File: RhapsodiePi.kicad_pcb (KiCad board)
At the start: 2 copper layers, 85.2 x 56.1 mm, 209 parts, among them J1 Micro_SD_Card_Det, J2 Conn_02x05_Odd_Even, J3 USB_A_Stacked, J4 USB_A_Stacked, J6 RJ45_HR913550A, J7 AudioJack4, U1 MT3420C-mt3420c, U11 LM4871, U13 TPS65185RGZR, U2 MT3420C-mt3420c, U3 MT3420C-mt3420c, U4 X1000, U5 AP6212, U6 FE2.1, U7 RTL8201F, U8 M25PX32-VMW, U9 TFP410PAP, X1 SG-3030CM, Y1 12MHz, Y2 24MHz, Y3 32.768kHz

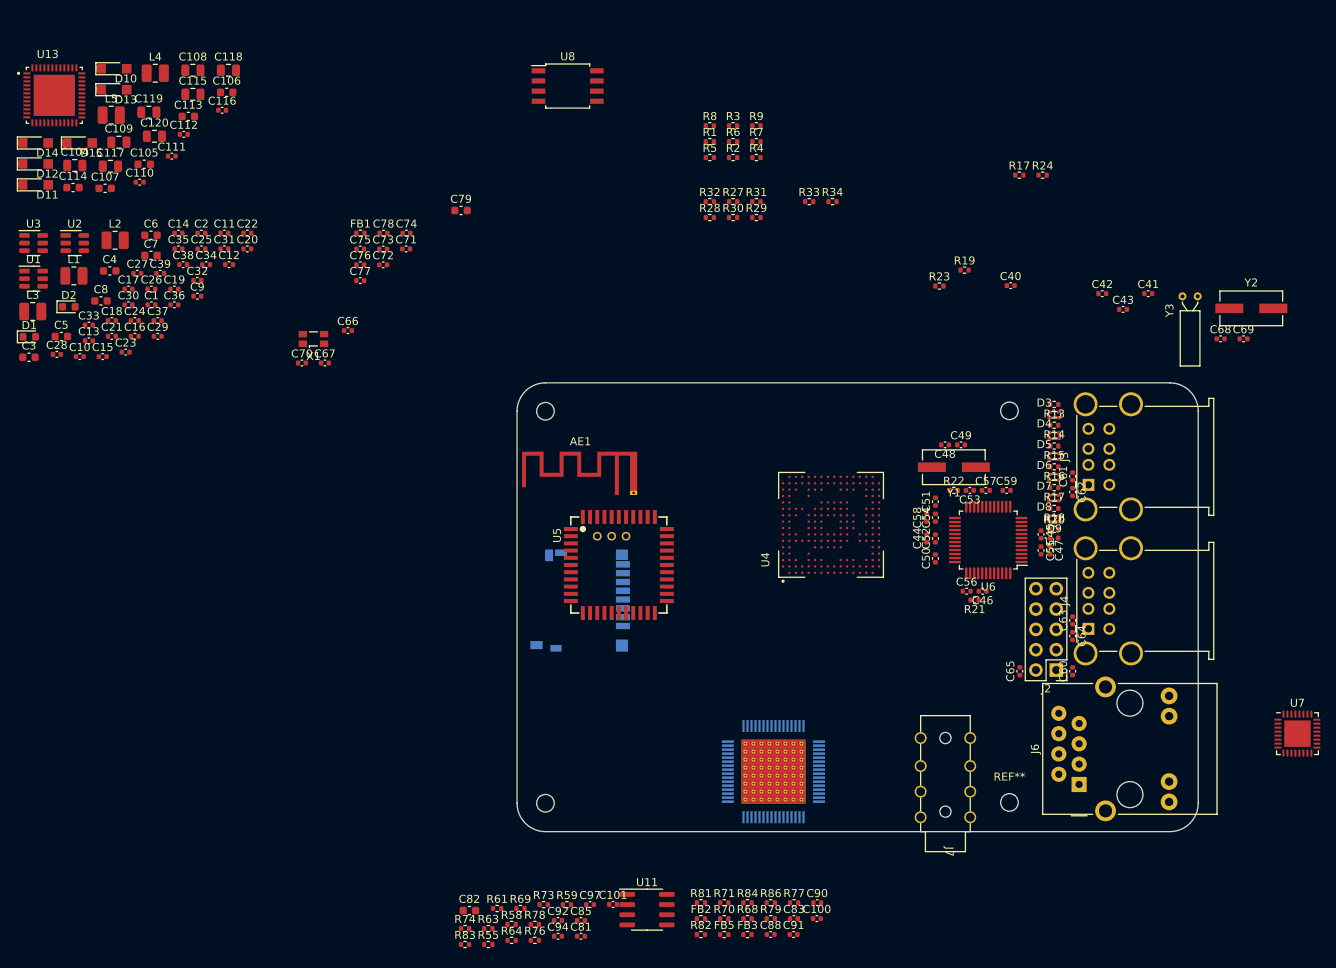
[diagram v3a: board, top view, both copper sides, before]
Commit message: Display Update
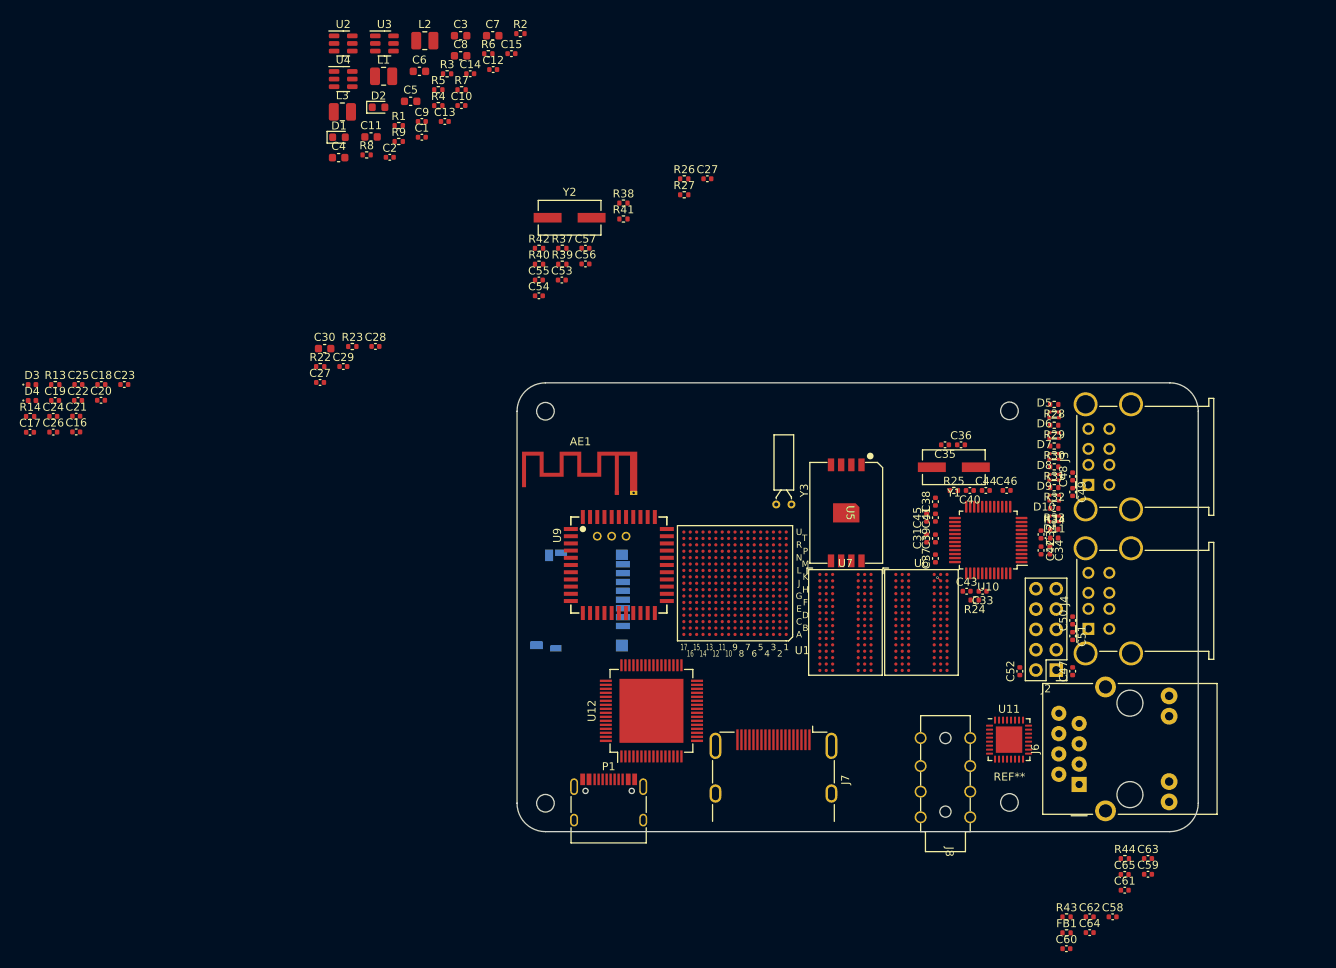
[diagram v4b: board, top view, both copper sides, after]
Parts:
- removed C100, C101, C73, C74, C85: 1µ, Capacitor_SMD:C_0402_1005Metric
- removed C104, C108, C109, C115, C117, C118, C119, C120: 4µ7, Capacitor_SMD:C_0805_2012Metric
- removed C105, C106, C107, C113, C114, C79, C82: 22µ, Capacitor_SMD:C_0603_1608Metric
- removed C110, C116, C71, C72, C75, C76, C77, C78, C81: 100n, Capacitor_SMD:C_0402_1005Metric
- removed C111, C112: 10n, Capacitor_SMD:C_0402_1005Metric
- removed the C27 at (36.8, 50.7)
- removed the C31 at (47.7, 47.6)
- removed the C32 at (44.3, 51.5)
- removed the C33 at (30.8, 57.1)
- removed the C34 at (45.4, 49.6)
- removed the C35 at (42.0, 47.6)
- removed the C36 at (41.5, 54.6)
- removed the C37 at (39.4, 56.6)
- removed the C38 at (42.6, 49.6)
- removed the C39 at (39.7, 50.7)
- removed the C40 at (146.0, 52.2)
- removed the C41 at (163.2, 53.2)
- removed the C42 at (157.5, 53.2)
- removed the C43 at (160.1, 55.2)
- removed C66, C67, C68, C69, C70: C, Capacitor_SMD:C_0402_1005Metric
- removed C83, C94, C97: 1n, Capacitor_SMD:C_0402_1005Metric
- removed C88, C90, C91, C92: 220p, Capacitor_SMD:C_0402_1005Metric
- removed the D10 at (33.9, 25.1)
- removed the D11 at (24.1, 39.6)
- removed D12, D13, D14, D15: D_Schottky, TheBrutzlers_Lib:SOD-123FL
- removed FB2, FB3, FB5: FerriteBead, Resistor_SMD:R_0402_1005Metric
- removed L4: 2µ2, Inductor_SMD:L_1008_2520Metric
- removed L5: 4µ7, Inductor_SMD:L_1008_2520Metric
- removed R17: 1K, Resistor_SMD:R_0402_1005Metric
- removed R19: 43.2, Resistor_SMD:R_0402_1005Metric
- removed the R24 at (150.0, 38.4)
- removed the R28 at (108.4, 43.7)
- removed the R29 at (114.2, 43.7)
- removed the R30 at (111.3, 43.7)
- removed the R31 at (114.2, 41.7)
- removed the R32 at (108.4, 41.7)
- removed the R33 at (120.8, 41.7)
- removed the R34 at (123.7, 41.7)
- removed R55: 2K2, Resistor_SMD:R_0402_1005Metric
- removed R58, R59, R61, R63, R64, R68, R69, R70, R71: 2K7, Resistor_SMD:R_0402_1005Metric
- removed R73, R74, R76, R81, R82: 10K, Resistor_SMD:R_0402_1005Metric
- removed R77, R78, R79: 20K, Resistor_SMD:R_0402_1005Metric
- removed R83, R84, R86: 0R, Resistor_SMD:R_0402_1005Metric
- removed U13: TPS65185RGZR, TheBrutzlers_Lib:QFN50P700X700X100-49N
- removed U8: M25PX32-VMW, Package_SO:SOIC-8W_5.3x5.3mm_P1.27mm
- removed the U9 at (116.3, 113.0)
- removed X1: SG-3030CM, Oscillator:Oscillator_SMD_SeikoEpson_SG3030CM
- added C27: 1µ, Capacitor_SMD:C_0402_1005Metric, F.Cu at (59.7, 64.3)
- added C27: 1µ, Capacitor_SMD:C_0402_1005Metric, F.Cu at (108.1, 38.8)
- added C53: C, Capacitor_SMD:C_0402_1005Metric, F.Cu at (89.9, 51.5)
- added C54: C, Capacitor_SMD:C_0402_1005Metric, F.Cu at (87.0, 53.5)
- added C55: C, Capacitor_SMD:C_0402_1005Metric, F.Cu at (87.0, 51.5)
- added C56: C, Capacitor_SMD:C_0402_1005Metric, F.Cu at (92.8, 49.5)
- added C57: C, Capacitor_SMD:C_0402_1005Metric, F.Cu at (92.8, 47.5)
- added C58: 100n, Capacitor_SMD:C_0402_1005Metric, F.Cu at (158.8, 131.1)
- added C59: 100n, Capacitor_SMD:C_0402_1005Metric, F.Cu at (163.2, 125.8)
- added C60: 1µ, Capacitor_SMD:C_0402_1005Metric, F.Cu at (153.0, 135.1)
- added C61: 1µ, Capacitor_SMD:C_0402_1005Metric, F.Cu at (160.3, 127.8)
- added C62: 100n, Capacitor_SMD:C_0402_1005Metric, F.Cu at (155.9, 131.1)
- added C63: 100n, Capacitor_SMD:C_0402_1005Metric, F.Cu at (163.2, 123.8)
- added C64: 100n, Capacitor_SMD:C_0402_1005Metric, F.Cu at (155.9, 133.1)
- added C65: 100n, Capacitor_SMD:C_0402_1005Metric, F.Cu at (160.3, 125.8)
- added D3: LED, LED_SMD:LED_0402_1005Metric, F.Cu at (23.7, 64.6)
- added D4: LED, LED_SMD:LED_0402_1005Metric, F.Cu at (23.7, 66.6)
- added J7: HDMI_A, Connector_HDMI:HDMI_A_Molex_208658-1001_Horizontal, F.Cu at (116.3, 112.2)
- added P1: USB_C_Plug, Connector_USB:USB_C_Receptacle_HRO_TYPE-C-31-M-12, F.Cu at (95.8, 118.0)
- added R13: 1K, Resistor_SMD:R_0402_1005Metric, F.Cu at (26.6, 64.6)
- added R14: 1K, Resistor_SMD:R_0402_1005Metric, F.Cu at (23.4, 68.5)
- added R22: 0R, Resistor_SMD:R_0402_1005Metric, F.Cu at (59.7, 62.3)
- added R26: 2K7, Resistor_SMD:R_0402_1005Metric, F.Cu at (105.2, 38.9)
- added R37: 1K, Resistor_SMD:R_0402_1005Metric, F.Cu at (90.0, 47.5)
- added R38: 100K, Resistor_SMD:R_0402_1005Metric, F.Cu at (97.6, 41.9)
- added R39: 100K, Resistor_SMD:R_0402_1005Metric, F.Cu at (90.0, 49.5)
- added R40: 1K, Resistor_SMD:R_0402_1005Metric, F.Cu at (87.0, 49.5)
- added R41: 100K, Resistor_SMD:R_0402_1005Metric, F.Cu at (97.6, 43.9)
- added R42: 1K, Resistor_SMD:R_0402_1005Metric, F.Cu at (87.0, 47.5)
- added R43: 1K, Resistor_SMD:R_0402_1005Metric, F.Cu at (153.0, 131.1)
- added R44: 1K, Resistor_SMD:R_0402_1005Metric, F.Cu at (160.3, 123.8)
- added U12: TFP410PAP, Package_QFP:HTQFP-64-1EP_10x10mm_P0.5mm_EP8x8mm, F.Cu at (101.1, 105.3)
- added U5: MKDN0xxxCL, TheBrutzlers_Lib:LGA-16_NAND, F.Cu at (125.5, 80.6)
- added U6: MT41K256M16TW, Package_BGA:BGA-96_9.0x13.0mm_Layout2x3x16_P0.8mm, F.Cu at (134.8, 94.3)
- C11, C30: value 100n -> 22µ; footprint Capacitor_SMD:C_0402_1005Metric -> Capacitor_SMD:C_0603_1608Metric
- C16, C24, C25, C26, C28: value 100n -> 1µ
- R23: value 2K7 -> 0R
- R5: value 200K -> 133K
- U1: value MT3420C-mt3420c -> IMX6UL; footprint Package_TO_SOT_SMD:SOT-23-6 -> TheBrutzlers_Lib:IMX6UL_BGA289
- U11: value LM4871 -> RTL8201F; footprint Package_SO:SOIC-8_3.9x4.9mm_P1.27mm -> Package_DFN_QFN:QFN-32-1EP_5x5mm_P0.5mm_EP3.3x3.3mm
- U4: value X1000 -> MT3420C-mt3420c; footprint TheBrutzlers_Lib:BGA256C80P16X16_1300X1300X130N -> Package_TO_SOT_SMD:SOT-23-6
- U7: value RTL8201F -> MT41K256M16TW; footprint Package_DFN_QFN:QFN-32-1EP_5x5mm_P0.5mm_EP3.3x3.3mm -> Package_BGA:BGA-96_9.0x13.0mm_Layout2x3x16_P0.8mm
- moved FB1 124.3 mm to (153.0, 133.1)
- moved U1 95.6 mm to (111.5, 89.4), turned to 180 degrees
- moved Y2 86.0 mm to (90.9, 43.7)
- moved U4 82.6 mm to (62.6, 26.4), turned to 0 degrees
- moved R23 73.8 mm to (63.7, 59.8)
- moved C3 67.3 mm to (77.2, 21.0)
- moved C15 63.6 mm to (83.6, 23.2)
- moved U7 58.2 mm to (125.3, 94.3)
- moved C10 57.1 mm to (77.3, 29.7)
- moved Y3 55.4 mm to (118.6, 79.5), turned to 180 degrees
- moved C8 54.4 mm to (77.2, 23.5)
- moved C5 52.6 mm to (71.0, 29.2)
- moved C13 52.3 mm to (75.3, 31.7)
- moved C7 50.8 mm to (81.3, 21.0)
- moved U3 50.5 mm to (67.7, 21.9)
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- renumbered C44 to C31, C45 to C32, C46 to C33, C47 to C34, C48 to C35, C49 to C36, C50 to C37, C51 to C38, C52 to C39, C53 to C40, C54 to C41, C55 to C42, C56 to C43, C57 to C44, C58 to C45, C59 to C46, C60 to C47, C61 to C48, C62 to C49, C63 to C50, C64 to C51, C65 to C52, D8 to D10, D9 to D11, D3 to D5, D4 to D6, D5 to D7, D6 to D8, D7 to D9, J7 to J8, R21 to R24, R22 to R25, R13 to R28, R14 to R29, R15 to R30, R16 to R31, R17 to R32, R18 to R33, R20 to R34, U6 to U10, U5 to U9
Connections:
- C10 pad 1: +1V8 -> AGND2
- C10 pad 2: AGND2 -> Net-(C10-Pad2)
- C11 pad 1: +3.3VA -> Net-(C10-Pad2)
- C12 pad 1: +1V2 -> AGND2
- C12 pad 2: AGND2 -> Net-(C10-Pad2)
- C13 pad 1: +1V8 -> Net-(C10-Pad2)
- C14 pad 1: +3.3VA -> AGND2
- C14 pad 2: AGND2 -> Net-(C10-Pad2)
- C15 pad 1: +1V2 -> AGND2
- C15 pad 2: AGND2 -> Net-(C10-Pad2)
- C16 pad 1: +1V8 -> +3V3
- C17 pad 1: +1V2 -> Net-(C17-Pad1)
- C18 pad 1: +1V8 -> Net-(C18-Pad1)
- C19 pad 1: +3V3 -> Net-(C18-Pad1)
- C20 pad 1: +1V2 -> Net-(C18-Pad1)
- C21 pad 1: +1V8 -> Net-(C18-Pad1)
- C22 pad 1: +3V3 -> Net-(C18-Pad1)
- C23 pad 1: +1V2 -> Net-(C18-Pad1)
- C24 pad 1: +1V8 -> +3V3
- C26 pad 1: +1V2 -> +3V3
- C28 pad 1: +3V3 -> Net-(C28-Pad1)
- C29 pad 1: +1V2 -> Net-(C29-Pad1)
- C30 pad 1: +1V8 -> Net-(C29-Pad1)
- C7 pad 1: +1V8 -> +1V4
- C9 pad 1: +1V2 -> AGND2
- C9 pad 2: AGND2 -> Net-(C10-Pad2)
- FB1 pad 2: Net-(C74-Pad2) -> Net-(C61-Pad2)
- J1 pad 1: Net-(J1-Pad1) -> /Memory/SD1_DAT2
- J1 pad 2: Net-(J1-Pad2) -> /Memory/SD1_DAT3
- J1 pad 3: Net-(J1-Pad3) -> /Memory/SD1_CMD
- J1 pad 5: Net-(J1-Pad5) -> /Memory/SD1_CLK
- J1 pad 7: Net-(J1-Pad7) -> /Memory/SD1_DAT0
- J1 pad 8: Net-(J1-Pad8) -> /Memory/SD1_DAT1
- L2 pad 2: +1V8 -> +1V4
- R23 pad 1: AGND2 -> Net-(C28-Pad1)
- R23 pad 2: Net-(R23-Pad2) -> +5V
- R27 pad 1: +3V3 -> Net-(R27-Pad1)
- R27 pad 2: Net-(R27-Pad2) -> AGND2
- R5 pad 1: +1V8 -> +1V4
- R9 pad 1: +1V8 -> +1V4
- U10 pad 27: Net-(R23-Pad2) -> Net-(R26-Pad2)
- U10 pad 29: Net-(U4-PadT12) -> Net-(U1-PadT13)
- U10 pad 30: Net-(U4-PadR12) -> Net-(U1-PadU13)
- U10 pad 46: Net-(R24-Pad1) -> Net-(R27-Pad1)
- U11 pad 3: Net-(R73-Pad2) -> Net-(J6-Pad1)
- U11 pad 4: Net-(R74-Pad2) -> Net-(J6-Pad3)
- U11 pad 5: Net-(R77-Pad2) -> Net-(J6-Pad4)
- U11 pad 6: Net-(C100-Pad2) -> Net-(J6-Pad6)
- U11 pad 7: AGND2 -> Net-(C61-Pad2)
- U11 pad 8: unconnected-(U11-Pad8) -> /Network/ENET1_MII/RMII_MODE
- U2 pad 1: unconnected-(U2-Pad1) -> Net-(C1-Pad1)
- U2 pad 3: Net-(L2-Pad1) -> Net-(L1-Pad1)
- U2 pad 6: Net-(R5-Pad2) -> Net-(R3-Pad2)
- U3 pad 1: Net-(C2-Pad1) -> +5V
- U3 pad 3: Net-(L3-Pad1) -> Net-(L2-Pad1)
- U3 pad 6: Net-(R7-Pad2) -> Net-(R5-Pad2)
- U9 pad 14: Net-(U4-PadF3) -> Net-(U8-PadF3)
- U9 pad 15: Net-(U4-PadE3) -> Net-(U8-PadE3)
- U9 pad 16: Net-(U4-PadF2) -> Net-(U8-PadF2)
- U9 pad 17: Net-(U4-PadE1) -> Net-(U8-PadE1)
- U9 pad 18: Net-(U4-PadD1) -> Net-(U8-PadD1)
- U9 pad 19: Net-(U4-PadE2) -> Net-(U8-PadE2)
- Y2 pad 2: Net-(C66-Pad2) -> Net-(C53-Pad2)
- Y3 pad 1: Net-(C68-Pad2) -> Net-(C55-Pad2)
- Y3 pad 2: Net-(C69-Pad2) -> Net-(C56-Pad2)
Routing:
- net /Memory/MMDC_D14: track 0.00 -> 0.57 mm, vias 0 -> 1
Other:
- board text removed: "Camera Interface"
